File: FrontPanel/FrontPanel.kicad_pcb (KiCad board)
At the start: 2 copper layers, 105.2 x 70.9 mm, 72 parts, among them SW1 Channel 1, SW10 5, SW11 2, SW12 0, SW13 9, SW14 6, SW15 3, SW16 Backspace, SW17 Voltage 1, SW18 Current 1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

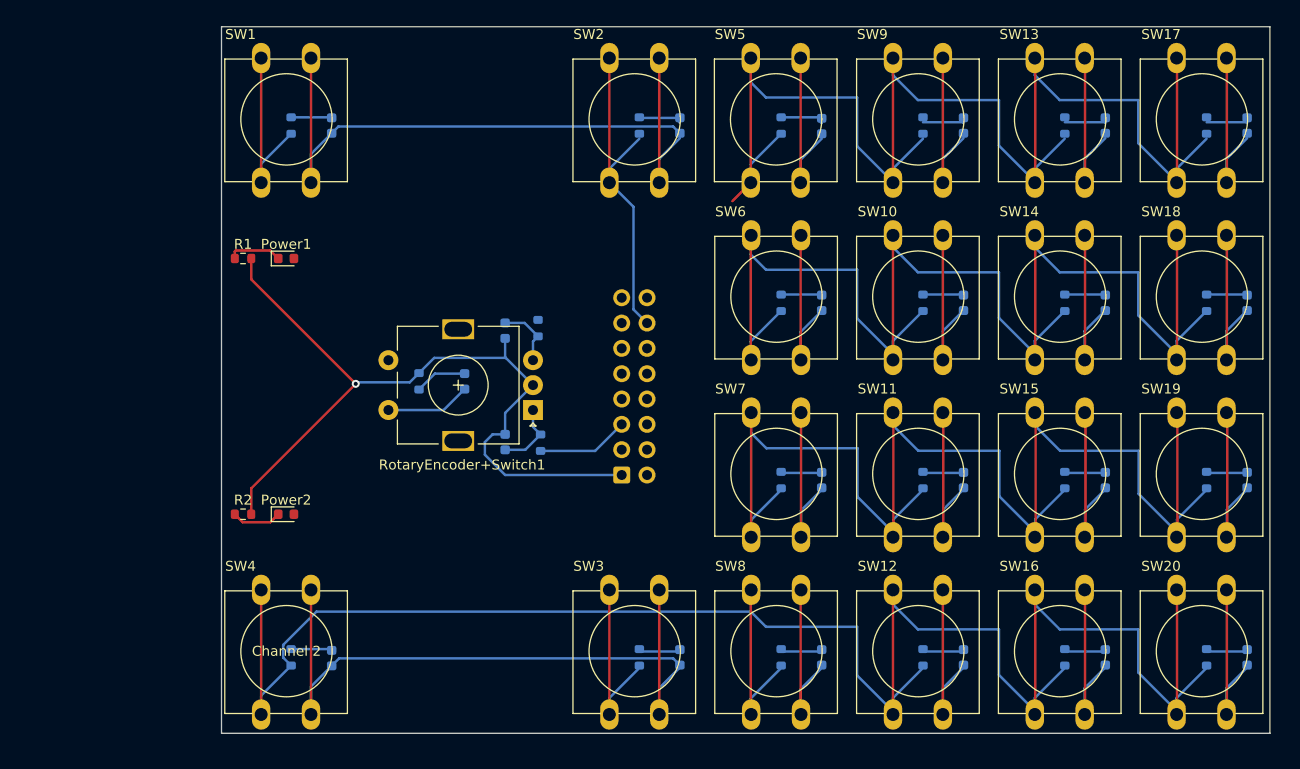
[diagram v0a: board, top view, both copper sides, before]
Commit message: Front panel routing done, drc only shows silkscreen warnings
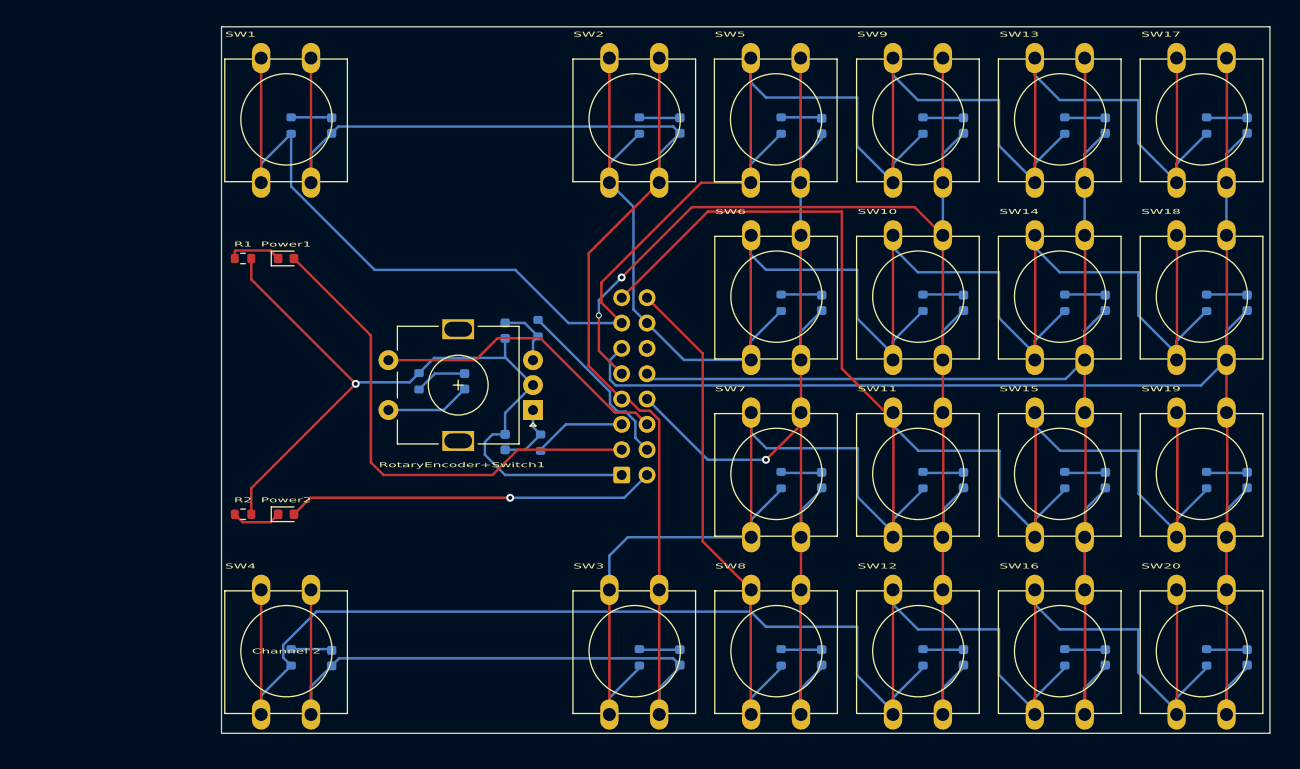
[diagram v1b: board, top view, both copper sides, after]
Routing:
- net Net-(C_DBC_17-Pad2): track 73.3 -> 156.4 mm
- net Net-(SW13-Pad1): track 167.8 -> 237.1 mm
- net Net-(Front_Panel2-Pad15): track 163.3 -> 230.0 mm
- net Net-(C_DBC_10-Pad2): track 73.3 -> 137.5 mm, vias 0 -> 2
- net Net-(C_DBC_13-Pad2): track 73.3 -> 134.5 mm
- net Net-(Front_Panel2-Pad3): track 0.00 -> 50.4 mm
- net Net-(C_DBC_1-Pad2): track 144.2 -> 192.4 mm
- net Net-(Front_Panel2-Pad2): track 0.00 -> 37.0 mm, vias 0 -> 1
- net Net-(C_DBC_5-Pad2): track 73.1 -> 109.9 mm, vias 0 -> 1
- net Net-(Front_Panel2-Pad16): track 214.0 -> 247.9 mm
- net Net-(Front_Panel2-Pad6): track 0.00 -> 30.4 mm
- net Net-(Front_Panel2-Pad4): track 0.00 -> 18.0 mm
- net Net-(Front_Panel2-Pad14): track 179.0 -> 190.8 mm

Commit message: Rerouted front panel with less vias
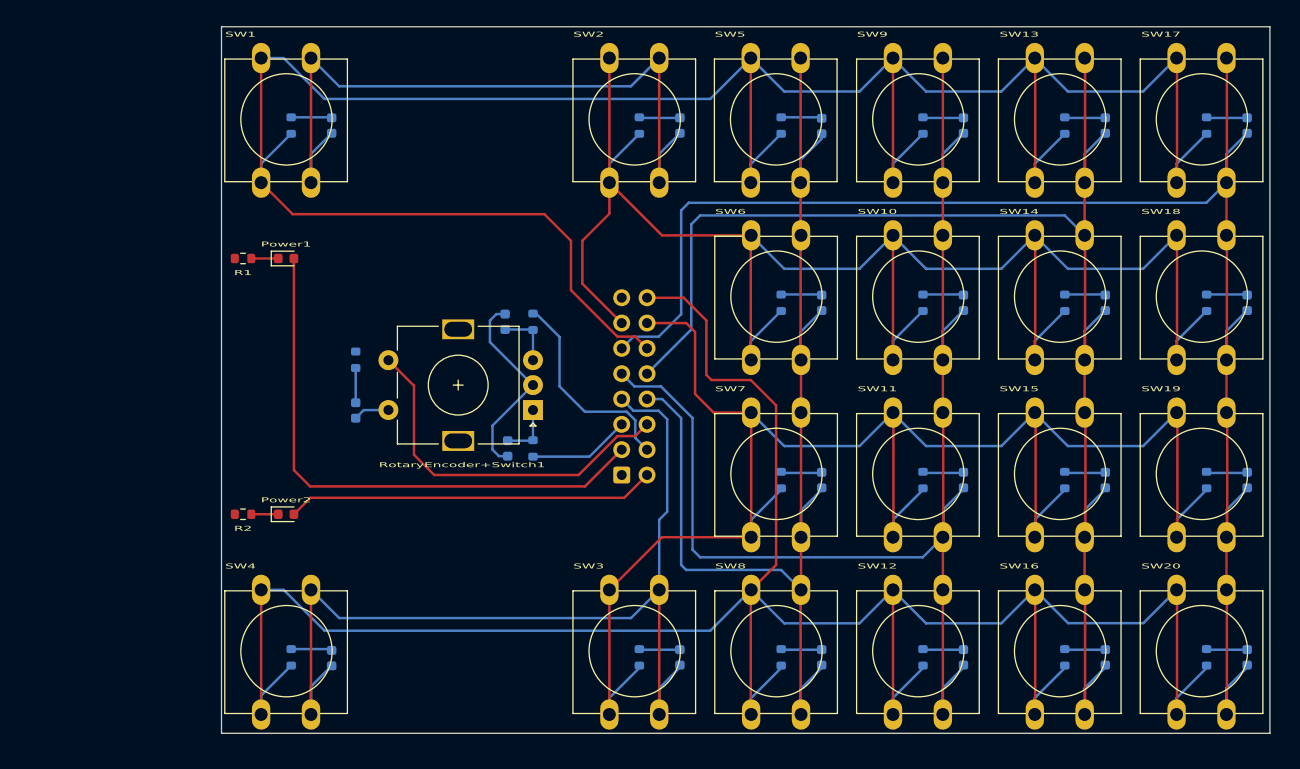
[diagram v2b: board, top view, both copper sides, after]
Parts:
- moved C_DBC_23 11.3 mm to (190.5, 52.5)
- moved R_DBC_23 6.71 mm to (190.5, 47.4)
- moved R_DBC_22 0.95 mm to (208.3, 56.3)
- moved C_DBC_21 0.89 mm to (205.5, 43.6), turned to -90 degrees
- moved R_DBC_21 0.81 mm to (208.3, 43.6)
- moved C_DBC_22 0.68 mm to (205.7, 56.3), turned to -90 degrees
- turned R1 to 180 degrees
- turned R2 to 180 degrees
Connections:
- Front_Panel2 pad 12: unconnected-(Front_Panel2-Pad12) -> Net-(R_DBC_13-Pad1)
- Front_Panel2 pad 13: Net-(SW13-Pad1) -> Net-(R_DBC_14-Pad1)
- Front_Panel2 pad 14: Net-(Front_Panel2-Pad14) -> Net-(R_DBC_15-Pad1)
- Front_Panel2 pad 15: Net-(Front_Panel2-Pad15) -> Net-(C_DBC_21-Pad1)
- R_DBC_1 pad 1: Net-(SW13-Pad1) -> Net-(R_DBC_13-Pad1)
- R_DBC_10 pad 1: Net-(Front_Panel2-Pad14) -> Net-(R_DBC_14-Pad1)
- R_DBC_11 pad 1: Net-(Front_Panel2-Pad15) -> Net-(R_DBC_15-Pad1)
- R_DBC_13 pad 1: Net-(SW13-Pad1) -> Net-(R_DBC_13-Pad1)
- R_DBC_14 pad 1: Net-(Front_Panel2-Pad14) -> Net-(R_DBC_14-Pad1)
- R_DBC_15 pad 1: Net-(Front_Panel2-Pad15) -> Net-(R_DBC_15-Pad1)
- R_DBC_17 pad 1: Net-(SW13-Pad1) -> Net-(R_DBC_13-Pad1)
- R_DBC_18 pad 1: Net-(Front_Panel2-Pad14) -> Net-(R_DBC_14-Pad1)
- R_DBC_19 pad 1: Net-(Front_Panel2-Pad15) -> Net-(R_DBC_15-Pad1)
- R_DBC_2 pad 1: Net-(Front_Panel2-Pad14) -> Net-(R_DBC_14-Pad1)
- R_DBC_3 pad 1: Net-(Front_Panel2-Pad15) -> Net-(R_DBC_15-Pad1)
- R_DBC_5 pad 1: Net-(SW13-Pad1) -> Net-(R_DBC_13-Pad1)
- R_DBC_6 pad 1: Net-(Front_Panel2-Pad14) -> Net-(R_DBC_14-Pad1)
- R_DBC_7 pad 1: Net-(Front_Panel2-Pad15) -> Net-(R_DBC_15-Pad1)
- R_DBC_9 pad 1: Net-(SW13-Pad1) -> Net-(R_DBC_13-Pad1)
- SW1 pad 1: Net-(SW13-Pad1) -> Net-(R_DBC_13-Pad1)
- SW10 pad 1: Net-(Front_Panel2-Pad14) -> Net-(R_DBC_14-Pad1)
- SW11 pad 1: Net-(Front_Panel2-Pad15) -> Net-(R_DBC_15-Pad1)
- SW13 pad 1: Net-(SW13-Pad1) -> Net-(R_DBC_13-Pad1)
- SW14 pad 1: Net-(Front_Panel2-Pad14) -> Net-(R_DBC_14-Pad1)
- SW15 pad 1: Net-(Front_Panel2-Pad15) -> Net-(R_DBC_15-Pad1)
- SW17 pad 1: Net-(SW13-Pad1) -> Net-(R_DBC_13-Pad1)
- SW18 pad 1: Net-(Front_Panel2-Pad14) -> Net-(R_DBC_14-Pad1)
- SW19 pad 1: Net-(Front_Panel2-Pad15) -> Net-(R_DBC_15-Pad1)
- SW2 pad 1: Net-(Front_Panel2-Pad14) -> Net-(R_DBC_14-Pad1)
- SW3 pad 1: Net-(Front_Panel2-Pad15) -> Net-(R_DBC_15-Pad1)
- SW5 pad 1: Net-(SW13-Pad1) -> Net-(R_DBC_13-Pad1)
- SW6 pad 1: Net-(Front_Panel2-Pad14) -> Net-(R_DBC_14-Pad1)
- SW7 pad 1: Net-(Front_Panel2-Pad15) -> Net-(R_DBC_15-Pad1)
- SW9 pad 1: Net-(SW13-Pad1) -> Net-(R_DBC_13-Pad1)
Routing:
- net Net-(R_DBC_13-Pad1): track 0.00 -> 252.8 mm
- net Net-(SW13-Pad1): track 237.1 -> 0.00 mm
- net Net-(Front_Panel2-Pad15): track 230.0 -> 0.00 mm
- net Net-(Front_Panel2-Pad14): track 190.8 -> 0.00 mm
- net Net-(R_DBC_15-Pad1): track 0.00 -> 180.2 mm
- net Net-(R_DBC_14-Pad1): track 0.00 -> 179.3 mm
- net Net-(C_DBC_21-Pad1): track 80.6 -> 20.0 mm, vias 1 -> 0
- net Net-(C_DBC_1-Pad2): track 192.4 -> 171.7 mm
- net Net-(C_DBC_5-Pad2): track 109.9 -> 122.6 mm, vias 1 -> 0
- net Net-(C_DBC_13-Pad2): track 134.5 -> 147.1 mm
- net Net-(R_DBC_16-Pad1): track 247.9 -> 239.1 mm
- net Net-(Front_Panel2-Pad11): track 156.4 -> 163.2 mm
- net Net-(Front_Panel2-Pad6): track 30.4 -> 36.9 mm
- net Net-(Front_Panel2-Pad3): track 50.4 -> 56.3 mm
- net Net-(C_DBC_23-Pad2): track 8.51 -> 3.62 mm
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
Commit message: Alligned trace grid on front panel
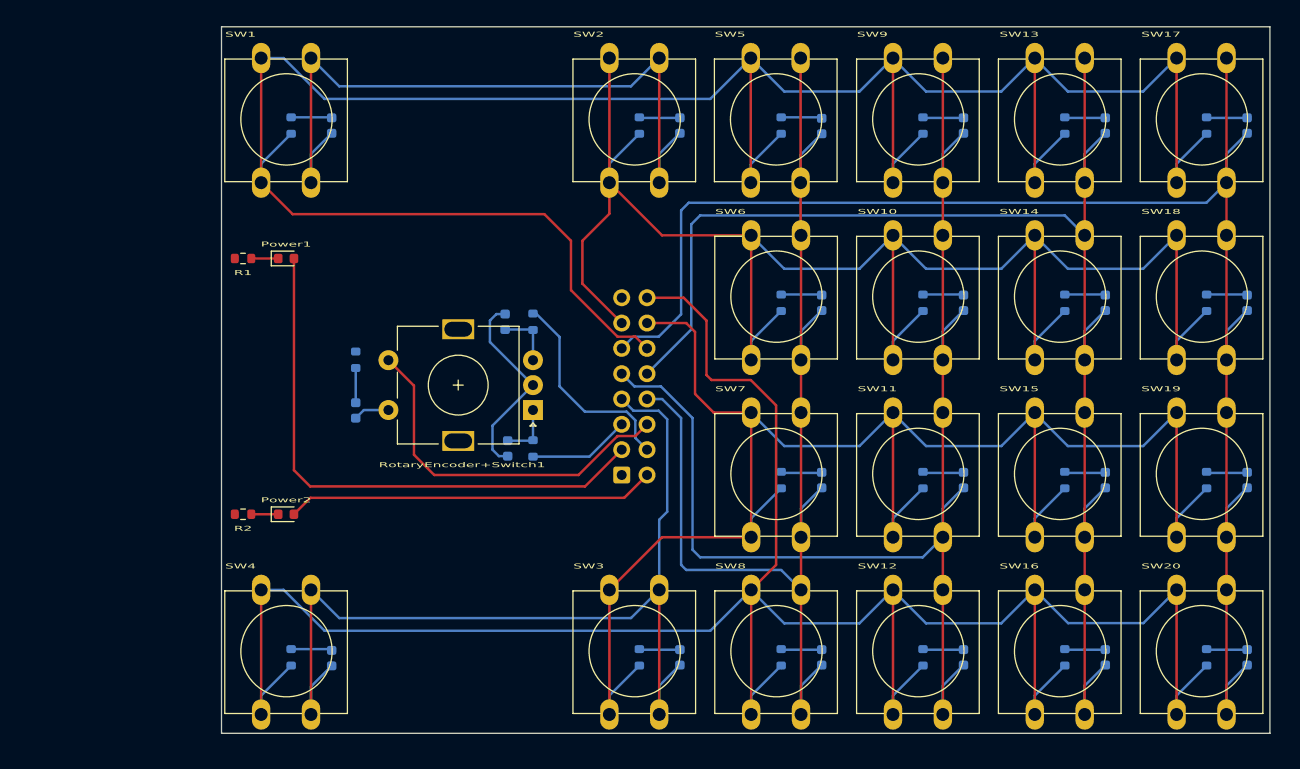
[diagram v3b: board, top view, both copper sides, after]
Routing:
- net Net-(C_DBC_5-Pad2): track 122.6 -> 121.4 mm

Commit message: Finialized the Front Panel
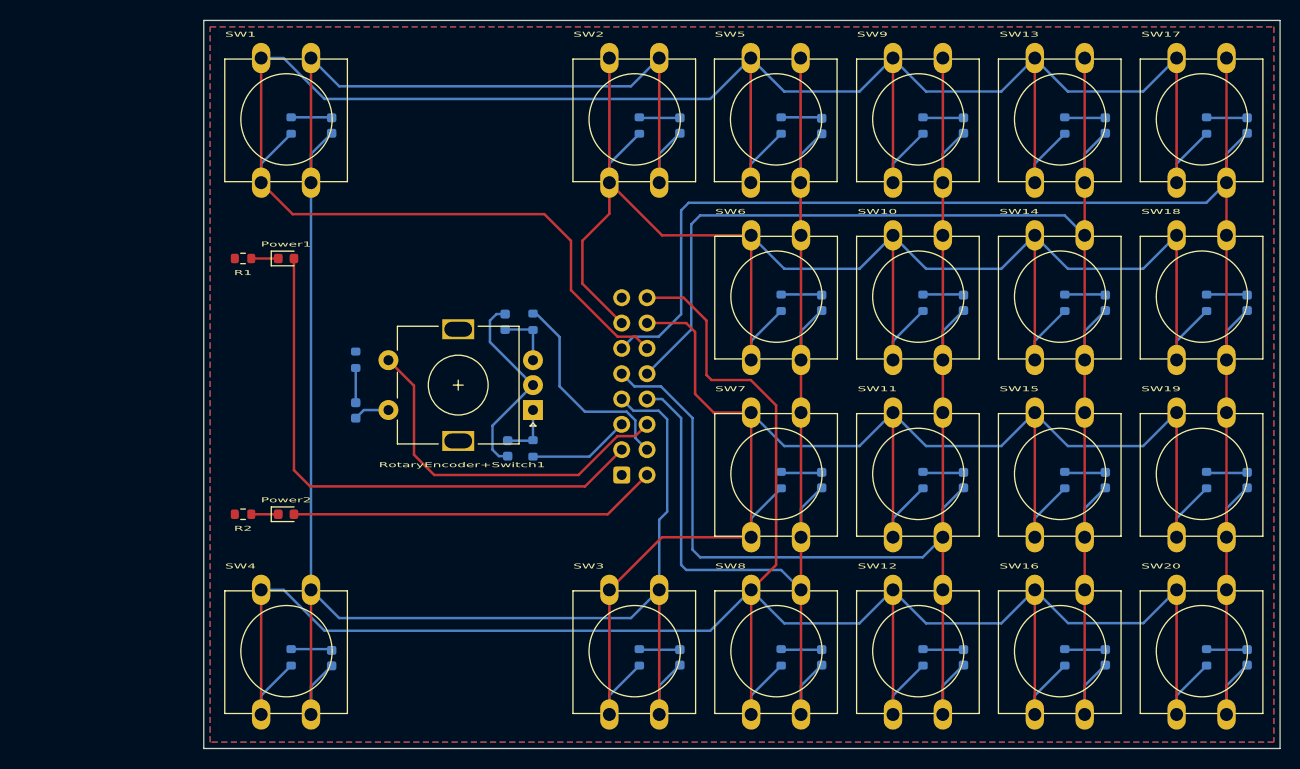
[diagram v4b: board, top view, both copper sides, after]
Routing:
- net Net-(C_DBC_1-Pad2): track 171.2 -> 212.0 mm
- added copper zone on B.Cu, net Net-(C_DBC_21-Pad1)
- added copper zone on F.Cu, net Net-(C_DBC_21-Pad1)
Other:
- board size 105.2 x 70.9 mm -> 107.9 x 73 mm
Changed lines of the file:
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@@
     )
   )
-  (gr_line (start 177.038 13.97) (end 282.194 13.97) (layer "Edge.Cuts") (width 0.1))
-  (gr_line (start 177.038 13.97) (end 177.038 84.836) (layer "Edge.Cuts") (width 0.1))
-  (gr_line (start 282.194 13.97) (end 282.194 84.836) (layer "Edge.Cuts") (width 0.1))
-  (gr_line (start 282.194 84.836) (end 177.038 84.836) (layer "Edge.Cuts") (width 0.1))
-  (segment (start 185.9535 61.214) (end 217.4335 61.214) (width 0.25) (layer "F.Cu") (net 1))
-  (segment (start 184.3025 62.865) (end 185.9535 61.214) (width 0.25) (layer "F.Cu") (net 1))
-  (segment (start 217.4335 61.214) (end 219.7195 58.928) (width 0.25) (layer "F.Cu") (net 1))
+  (gr_line (start 175.26 13.335) (end 283.21 13.335) (layer "Edge.Cuts") (width 0.1))
+  (gr_line (start 175.26 13.335) (end 175.26 86.36) (layer "Edge.Cuts") (width 0.1))
+  (gr_line (start 283.21 13.335) (end 283.21 86.36) (layer "Edge.Cuts") (width 0.1))
+  (gr_line (start 283.21 86.36) (end 175.26 86.36) (layer "Edge.Cuts") (width 0.1))
+  (segment (start 215.7825 62.865) (end 219.7195 58.928) (width 0.25) (layer "F.Cu") (net 1))
+  (segment (start 184.3025 62.865) (end 215.7825 62.865) (width 0.25) (layer "F.Cu") (net 1))
   (segment (start 217.1795 56.388) (end 213.4965 60.071) (width 0.25) (layer "F.Cu") (net 2))
   (segment (start 184.3025 58.4455) (end 184.3025 37.211) (width 0.25) (layer "F.Cu") (net 2))
@@
   (segment (start 186.015 80.139) (end 186.015 82.948) (width 0.25) (layer "B.Cu") (net 7))
   (segment (start 220.94 80.063) (end 220.94 82.948) (width 0.25) (layer "B.Cu") (net 7))
+  (segment (start 186.015 29.608) (end 186.015 70.448) (width 0.25) (layer "B.Cu") (net 7))
   (segment (start 186.015 70.448) (end 188.846 73.279) (width 0.25) (layer "B.Cu") (net 7))
   (segment (start 218.106 19.939) (end 220.937 17.108) (width 0.25) (layer "B.Cu") (net 7))
@@
   (segment (start 187.371817 74.549) (end 226.063 74.549) (width 0.25) (layer "B.Cu") (net 41))
   (segment (start 261.951 73.787) (end 258.612 70.448) (width 0.25) (layer "B.Cu") (net 41))
+  (zone (net 33) (net_name "Net-(C_DBC_21-Pad1)") (layers F&B.Cu) (hatch edge 0.508)
+    (connect_pads thru_hole_only (clearance 0.508))
+    (min_thickness 0.254) (filled_areas_thickness no)
+    (fill yes (thermal_gap 0.508) (thermal_bridge_width 0.508) (smoothing chamfer) (radius 0.508))
+    (polygon
+      (pts
+        (xy 282.575 85.725)
+        (xy 175.895 85.725)
+        (xy 175.895 13.97)
+        (xy 282.575 13.97)
+      )
+    )
+  )
   (group "" (id 226872b6-fdcf-4bb9-ab05-273074e31281)
     (members

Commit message: Finialize Front Panel for realz
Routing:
- net Net-(R_DBC_16-Pad1): track 239.0 -> 174.4 mm
- net Net-(R_DBC_13-Pad1): track 252.8 -> 188.5 mm
- net Net-(R_DBC_15-Pad1): track 180.2 -> 116.0 mm
- net Net-(R_DBC_14-Pad1): track 179.3 -> 115.0 mm
- net Net-(C_DBC_5-Pad2): track 121.4 -> 70.6 mm
- net Net-(C_DBC_1-Pad2): track 212.0 -> 161.4 mm
- net Net-(Front_Panel2-Pad11): track 162.7 -> 112.2 mm
- net Net-(C_DBC_10-Pad2): track 137.8 -> 87.7 mm
- net Net-(C_DBC_13-Pad2): track 146.6 -> 96.8 mm

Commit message: Finialize the Front Panel for realz for realz
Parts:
- added REF**: MountingHole_4.3mm_M4, MountingHole:MountingHole_4.3mm_M4, F.Cu at (268.7, 26.9)
- added REF**: MountingHole_4.3mm_M4, MountingHole:MountingHole_4.3mm_M4, F.Cu at (182.4, 79.8)
- added REF**: MountingHole_4.3mm_M4, MountingHole:MountingHole_4.3mm_M4, F.Cu at (182.4, 27.0)
- added REF**: MountingHole_4.3mm_M4, MountingHole:MountingHole_4.3mm_M4, F.Cu at (268.7, 79.8)
- moved C_DBC_13 18.4 mm to (247.3, 23.9)
- moved C_DBC_14 18.4 mm to (247.3, 41.7)
- moved C_DBC_15 18.4 mm to (247.3, 59.4)
- moved C_DBC_16 18.4 mm to (247.3, 77.2)
- moved C_DBC_17 18.4 mm to (261.5, 23.9)
- moved C_DBC_18 18.4 mm to (261.5, 41.7)
- moved C_DBC_19 18.4 mm to (261.5, 59.4)
- moved C_DBC_20 18.4 mm to (261.5, 77.2)
- moved SW13 18.4 mm to (240.2, 29.6)
- moved SW14 18.4 mm to (240.2, 47.4)
- moved SW15 18.4 mm to (240.2, 65.2)
- moved SW16 18.4 mm to (240.2, 82.9)
- moved C_DBC_1 18.4 mm to (169.7, 23.9)
- moved C_DBC_10 18.4 mm to (233.1, 41.7)
- moved C_DBC_11 18.4 mm to (233.1, 59.4)
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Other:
- board size 107.9 x 73 mm -> 117.2 x 73 mm
